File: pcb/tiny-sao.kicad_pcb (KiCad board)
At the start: 2 copper layers, 20 x 20 mm, 5 parts, among them J1 Conn_02x02_Counter_Clockwise, SW1 SW_Push, U1 ATtiny45-20SU

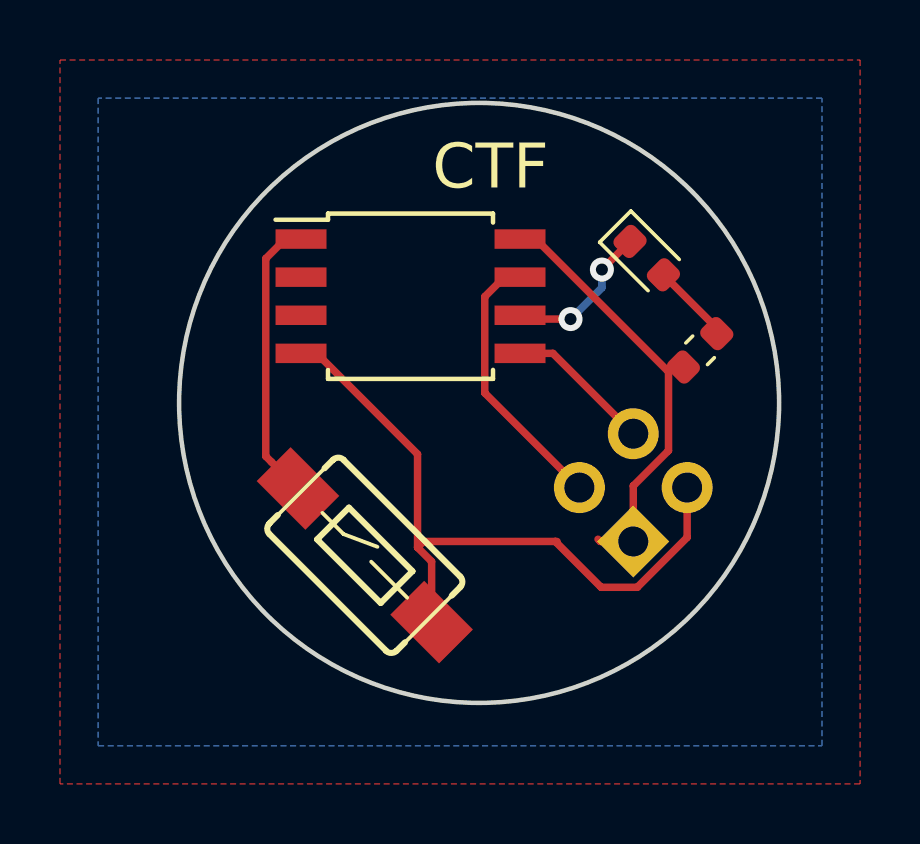
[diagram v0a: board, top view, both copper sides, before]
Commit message: fix(pcb): SCL and SDA were crossed
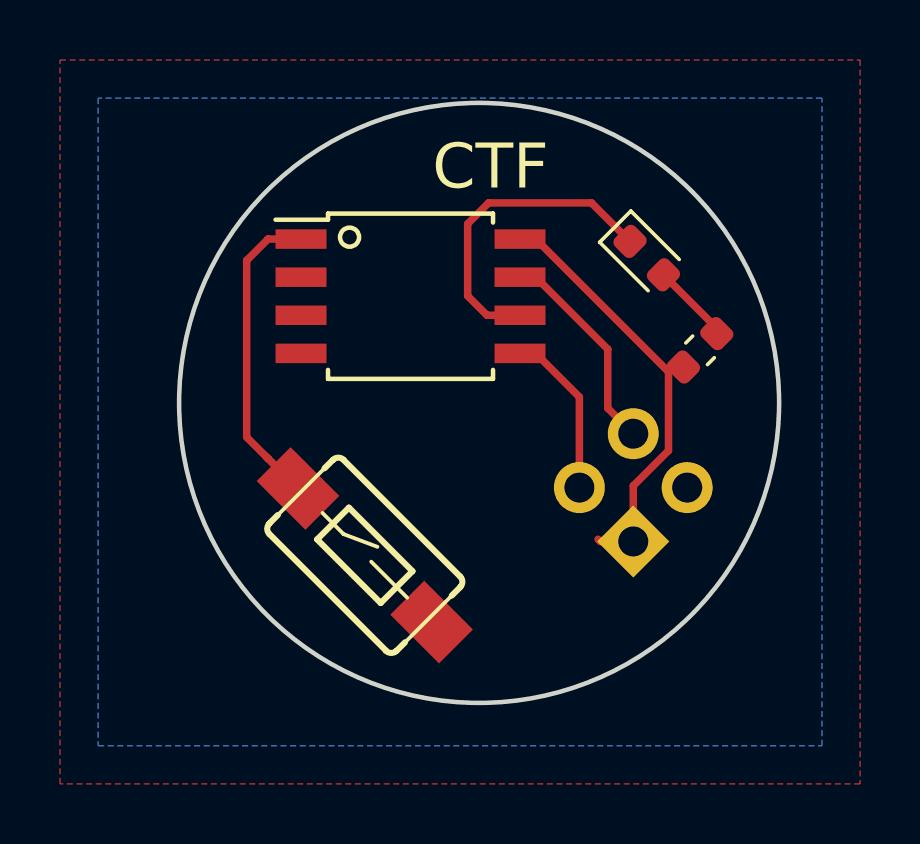
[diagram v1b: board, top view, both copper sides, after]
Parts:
- J1: value Conn_02x02_Counter_Clockwise -> Male_02x02
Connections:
- J1 pad 3: /SCL -> /SDA
- J1 pad 4: /SDA -> /SCL
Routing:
- net GND: track 23.2 -> 0.53 mm
- net Net-(D1-Pad1): track 5.15 -> 10.8 mm, vias 2 -> 0
- net Net-(SW1-Pad1): track 9.55 -> 11.1 mm
- net /SCL: track 9.11 -> 7.61 mm
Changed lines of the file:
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@@
-(kicad_pcb (version 20171130) (host pcbnew "(5.0.2)-1")
+(kicad_pcb (version 20171130) (host pcbnew "(5.1.4)-1")
   (general
     (thickness 1.6)
-    (drawings 2)
-    (tracks 42)
+    (drawings 3)
+    (tracks 35)
     (zones 0)
     (modules 5)
@@
     (zone_45_only no)
     (trace_min 0.2)
-    (segment_width 0.2)
-    (edge_width 0.15)
     (via_size 0.8)
     (via_drill 0.4)
@@
     (uvia_min_size 0.2)
     (uvia_min_drill 0.1)
+    (edge_width 0.15)
+    (segment_width 0.2)
     (pcb_text_width 0.3)
     (pcb_text_size 1.5 1.5)
@@
       (effects (font (size 1 1) (thickness 0.15)) (justify mirror))
     )
-    (fp_text value Conn_02x02_Counter_Clockwise (at 1.27 -4.87 45) (layer B.Fab)
+    (fp_text value Male_02x02 (at 1.27 -4.87 45) (layer B.Fab)
       (effects (font (size 1 1) (thickness 0.15)) (justify mirror))
     )
@@
       (net 2 GND))
     (pad 3 thru_hole oval (at 0 -2.54 45) (size 1.7 1.7) (drill 1) (layers *.Cu *.Mask)
+      (net 4 /SDA))
+    (pad 4 thru_hole oval (at 2.54 -2.54 45) (size 1.7 1.7) (drill 1) (layers *.Cu *.Mask)
       (net 3 /SCL))
-    (pad 4 thru_hole oval (at 2.54 -2.54 45) (size 1.7 1.7) (drill 1) (layers *.Cu *.Mask)
-      (net 4 /SDA))
     (model ${KISYS3DMOD}/Connector_PinHeader_2.54mm.3dshapes/PinHeader_2x02_P2.54mm_Vertical.wrl
       (at (xyz 0 0 0))
@@
     )
   )
+  (gr_circle (center 125.222 92.2655) (end 125.476 92.456) (layer F.SilkS) (width 0.15))
   (gr_text CTF (at 129.921 89.916) (layer F.SilkS)
     (effects (font (size 1.5 1.5) (thickness 0.3)))
@@
   (segment (start 136.013657 96.594347) (end 135.854002 96.754002) (width 0.25) (layer F.Cu) (net 1))
   (segment (start 136.349153 96.594347) (end 136.013657 96.594347) (width 0.25) (layer F.Cu) (net 1))
-  (segment (start 127.488601 99.498601) (end 127.488601 102.609001) (width 0.25) (layer F.Cu) (net 2))
-  (segment (start 124.129 96.139) (end 127.488601 99.498601) (width 0.25) (layer F.Cu) (net 2) (status 10))
   (segment (start 123.604 96.139) (end 124.129 96.139) (width 0.25) (layer F.Cu) (net 2) (status 30))
-  (segment (start 127.688601 102.409001) (end 127.488601 102.609001) (width 0.25) (layer F.Cu) (net 2))
-  (segment (start 133.607092 103.936093) (end 132.08 102.409001) (width 0.25) (layer F.Cu) (net 2))
-  (segment (start 134.813627 103.936093) (end 133.607092 103.936093) (width 0.25) (layer F.Cu) (net 2))
-  (segment (start 136.475052 102.274668) (end 134.813627 103.936093) (width 0.25) (layer F.Cu) (net 2))
-  (segment (start 136.475052 100.61295) (end 136.475052 102.274668) (width 0.25) (layer F.Cu) (net 2) (status 10))
-  (segment (start 132.139001 102.409001) (end 132.08 102.409001) (width 0.25) (layer F.Cu) (net 2))
-  (segment (start 132.08 102.409001) (end 127.688601 102.409001) (width 0.25) (layer F.Cu) (net 2))
-  (segment (start 127.957104 103.077504) (end 127.957104 105.097104) (width 0.25) (layer F.Cu) (net 2))
-  (segment (start 127.488601 102.609001) (end 127.957104 103.077504) (width 0.25) (layer F.Cu) (net 2))
   (segment (start 130.379 93.599) (end 130.904 93.599) (width 0.25) (layer F.Cu) (net 3) (status 30))
-  (segment (start 129.728999 94.249001) (end 130.379 93.599) (width 0.25) (layer F.Cu) (net 3) (status 20))
-  (segment (start 129.728999 97.458999) (end 129.728999 94.249001) (width 0.25) (layer F.Cu) (net 3))
-  (segment (start 132.88295 100.61295) (end 129.728999 97.458999) (width 0.25) (layer F.Cu) (net 3) (status 10))
-  (segment (start 131.429 96.139) (end 130.904 96.139) (width 0.25) (layer F.Cu) (net 4) (status 30))
-  (segment (start 132.001102 96.139) (end 130.904 96.139) (width 0.25) (layer F.Cu) (net 4) (status 20))
-  (segment (start 134.679001 98.816899) (end 132.001102 96.139) (width 0.25) (layer F.Cu) (net 4) (status 10))
+  (segment (start 131.429 93.599) (end 130.904 93.599) (width 0.25) (layer F.Cu) (net 3))
+  (segment (start 133.829002 95.999002) (end 131.429 93.599) (width 0.25) (layer F.Cu) (net 3))
+  (segment (start 134.679001 98.816899) (end 133.829002 97.9669) (width 0.25) (layer F.Cu) (net 3))
+  (segment (start 133.829002 97.9669) (end 133.829002 95.999002) (width 0.25) (layer F.Cu) (net 3))
+  (segment (start 131.429 96.139) (end 130.904 96.139) (width 0.25) (layer F.Cu) (net 4))
+  (segment (start 132.88295 97.59295) (end 131.429 96.139) (width 0.25) (layer F.Cu) (net 4))
+  (segment (start 132.88295 100.61295) (end 132.88295 97.59295) (width 0.25) (layer F.Cu) (net 4))
   (segment (start 122.619473 99.759473) (end 123.502896 100.642896) (width 0.25) (layer F.Cu) (net 5))
-  (segment (start 122.428999 99.568999) (end 122.619473 99.759473) (width 0.25) (layer F.Cu) (net 5))
-  (segment (start 122.428999 92.979001) (end 122.428999 99.568999) (width 0.25) (layer F.Cu) (net 5))
-  (segment (start 123.079 92.329) (end 122.428999 92.979001) (width 0.25) (layer F.Cu) (net 5))
   (segment (start 123.604 92.329) (end 123.079 92.329) (width 0.25) (layer F.Cu) (net 5))
-  (segment (start 134.571153 92.407153) (end 133.633306 93.345) (width 0.25) (layer F.Cu) (net 8))
-  (via (at 133.633306 93.345) (size 0.8) (drill 0.4) (layers F.Cu B.Cu) (net 8))
-  (segment (start 133.633306 93.345) (end 133.633306 93.950694) (width 0.25) (layer B.Cu) (net 8))
-  (via (at 132.588 94.996) (size 0.8) (drill 0.4) (layers F.Cu B.Cu) (net 8))
-  (segment (start 133.633306 93.950694) (end 132.588 94.996) (width 0.25) (layer B.Cu) (net 8))
+  (segment (start 122.504 92.329) (end 121.793 93.04) (width 0.25) (layer F.Cu) (net 5))
+  (segment (start 123.604 92.329) (end 122.504 92.329) (width 0.25) (layer F.Cu) (net 5))
+  (segment (start 121.793 98.933) (end 122.52325 99.66325) (width 0.25) (layer F.Cu) (net 5))
+  (segment (start 121.793 93.04) (end 121.793 98.933) (width 0.25) (layer F.Cu) (net 5))
+  (segment (start 122.428999 99.568999) (end 122.52325 99.66325) (width 0.25) (layer F.Cu) (net 5))
+  (segment (start 122.52325 99.66325) (end 122.619473 99.759473) (width 0.25) (layer F.Cu) (net 5))
   (segment (start 131.031 94.996) (end 130.904 94.869) (width 0.25) (layer F.Cu) (net 8))
-  (segment (start 132.588 94.996) (end 131.031 94.996) (width 0.25) (layer F.Cu) (net 8))
+  (segment (start 133.2865 91.1225) (end 134.571153 92.407153) (width 0.25) (layer F.Cu) (net 8))
+  (segment (start 129.8575 91.1225) (end 133.2865 91.1225) (width 0.25) (layer F.Cu) (net 8))
+  (segment (start 129.159 91.821) (end 129.8575 91.1225) (width 0.25) (layer F.Cu) (net 8))
+  (segment (start 129.159 94.224) (end 129.159 91.821) (width 0.25) (layer F.Cu) (net 8))
+  (segment (start 130.904 94.869) (end 129.804 94.869) (width 0.25) (layer F.Cu) (net 8))
+  (segment (start 129.804 94.869) (end 129.159 94.224) (width 0.25) (layer F.Cu) (net 8))
   (segment (start 137.462847 95.298847) (end 137.462847 95.480653) (width 0.25) (layer F.Cu) (net 9))
   (segment (start 135.684847 93.520847) (end 137.462847 95.298847) (width 0.25) (layer F.Cu) (net 9))
